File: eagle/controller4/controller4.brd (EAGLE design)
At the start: 47.9 x 64.8 mm, 62 parts, among them J4 USB-MICROB, J7 2X6 FEMALE, Q3 check_pins, X1 1501_04

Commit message: controller4 progress
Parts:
- removed HIGHSIDESWITCH: (no value), SparkFun-DiscreteSemi:TO220V
- added Q2: FDD4141TO252, transistor-fet:TO252
- moved SH 35.2 mm to (40.6, 13.6), turned to 180 degrees
- moved J5 17.8 mm to (43.2, 24.1)
- moved CONV_X_VCC 17.8 mm to (41.9, 35.6)
- moved J6 16.6 mm to (43.2, 16.5)
- moved R8 12.6 mm to (33.0, 10.2), turned to 90 degrees
- moved R9 8.98 mm to (30.5, 10.2), turned to 270 degrees
- moved DISP 2.54 mm to (25.4, 2.54)
- moved T_HSS 1.80 mm to (36.8, 34.3), turned to 270 degrees
- moved J3 1.27 mm to (39.4, 6.35)
- moved S1 1.27 mm to (43.9, 6.35)
- moved VD1 1.27 mm to (36.8, 55.9)
- moved X1 1.27 mm to (48.3, 61.0)
- moved R18 1.27 mm to (30.5, 33.0)
- moved SHTR 1.27 mm to (29.2, 62.2)
- moved R17 1.27 mm to (34.3, 29.2)
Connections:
- net BATT_VCC: now also Q2.2; no longer HIGHSIDESWITCH.3
- net CAM_OUT: now also Q2.3; no longer HIGHSIDESWITCH.2
- net N$36: now also Q2.1; no longer HIGHSIDESWITCH.1
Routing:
- net DISP_RST: track 46.1 -> 60.8 mm, vias 3 -> 1
- net GND: track 308.1 -> 298.0 mm
- net BATT_VCC: track 44.5 -> 35.9 mm, vias 0 -> 1
- net TX: track 28.6 -> 20.5 mm, vias 4 -> 0
- net GNDA: track 17.1 -> 9.05 mm
- net N$31: track 3.08 -> 10.4 mm
- net N$36: track 14.6 -> 8.84 mm
- net CAM_OUT: track 15.6 -> 9.88 mm
- net VCC: track 201.0 -> 197.2 mm
- net SCL: track 53.7 -> 57.1 mm, vias 2 -> 4
- net MOSI: track 24.5 -> 27.6 mm
- net BTN2: track 31.9 -> 33.7 mm
- net N$34: track 15.5 -> 14.1 mm
- net CAM_EN: track 6.91 -> 5.59 mm
- net N$6: track 5.14 -> 6.43 mm
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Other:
- board size 47.9 x 64.8 mm -> 46.7 x 64.8 mm

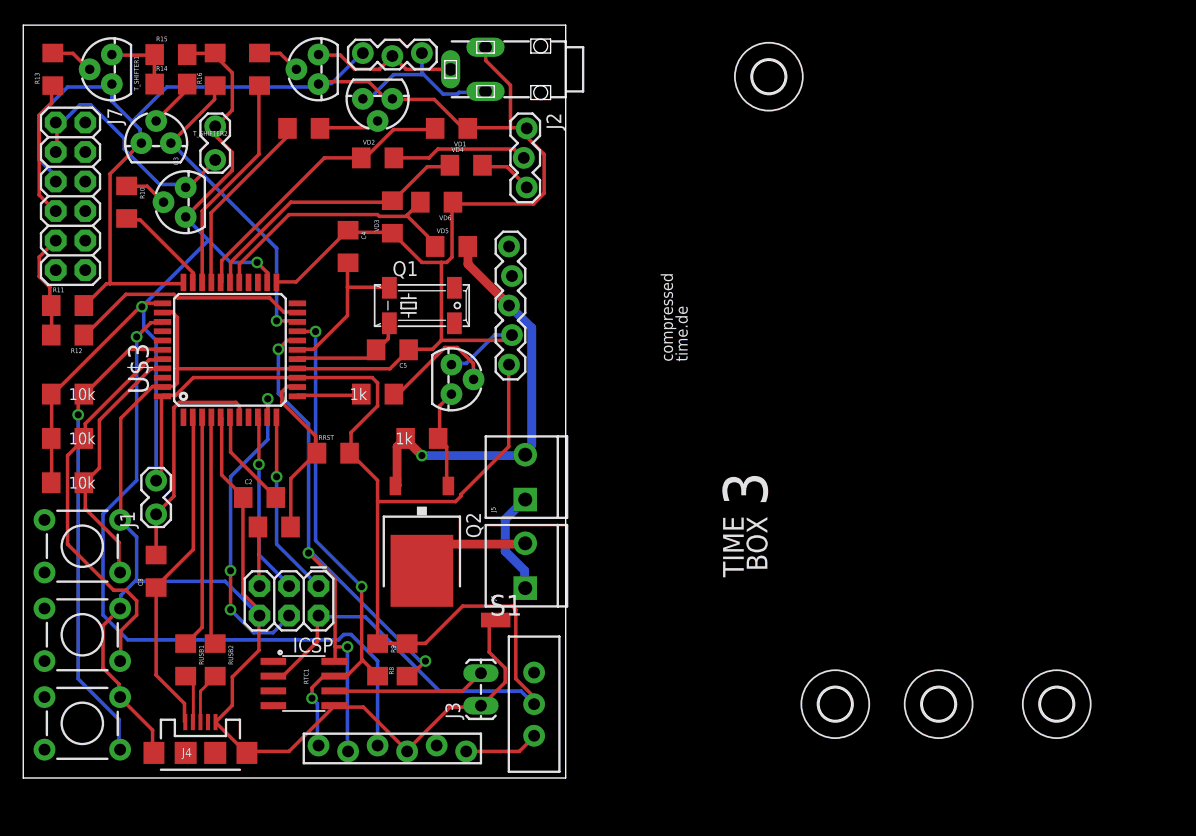
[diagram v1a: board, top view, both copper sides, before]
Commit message: controller4: added switch (battery -> USB)
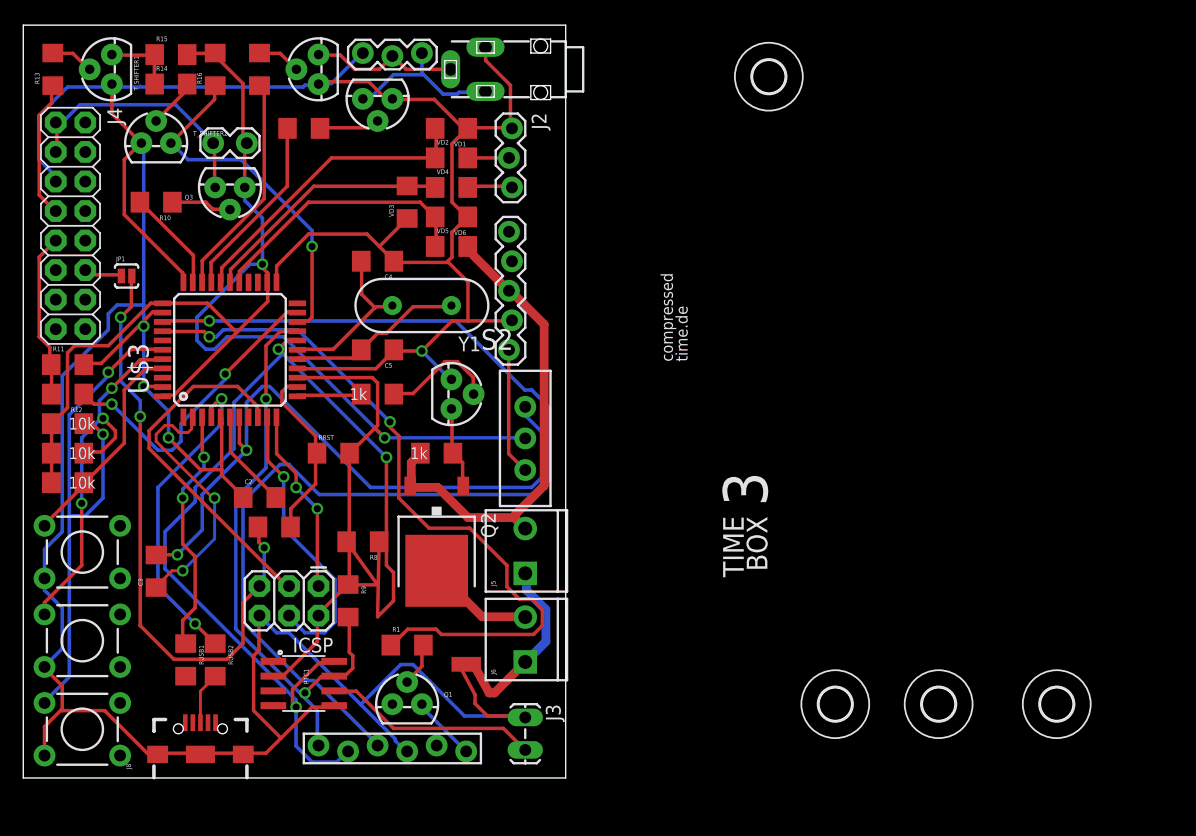
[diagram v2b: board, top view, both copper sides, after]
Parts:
- removed J1: (no value), SparkFun-Connectors:1X02_LOCK
- removed J7: 2X6 FEMALE, SparkFun-Connectors:2X6
- removed S1: (no value), SparkFun-Electromechanical:SWITCH-SPDT_LOCK.007S
- added J8: (no value), SparkFun-Connectors:USB-B-MICRO-SMD_V03
- added JP1: JUMPER-PAD-2-NOYES_SILK, SparkFun-Passives:PAD-JUMPER-2-NO_YES_SILK
- added R1: (no value), SparkFun-Resistors:1206
- added S2: (no value), SparkFun-Electromechanical:SWITCH-SPDT_LOCK.007S
- added Y1: (no value), SparkFun-FreqCtrl:HC49US
- J4: value USB-MICROB -> (none); device SparkFun-Connectors:USB-MICROB -> SparkFun-Connectors:2X8
- Q1: value (none) -> check_pins; device adafruit:MM20SS -> SparkFun-DiscreteSemi:TO-92
- moved J4 55.6 mm to (2.79, 56.4), turned to 270 degrees
- moved Q1 34.3 mm to (33.0, 6.35)
- moved R8 10.9 mm to (29.2, 20.3), turned to 180 degrees
- moved J6 6.35 mm to (43.2, 10.2)
- moved J5 6.35 mm to (43.2, 17.8)
- moved VD2 6.35 mm to (36.8, 53.3)
- moved R9 5.68 mm to (27.9, 15.2)
- moved R11 5.08 mm to (3.81, 35.6)
- moved R12 5.08 mm to (3.81, 33.0)
- moved SH 4.58 mm to (38.1, 9.78)
- moved J3 4.02 mm to (43.2, 5.08), turned to 270 degrees
- moved Q3 4.02 mm to (17.8, 50.8), turned to 180 degrees
- moved C4 2.84 mm to (30.5, 44.5), turned to 180 degrees
- moved RB3 2.54 mm to (3.81, 30.5)
- moved R10 2.54 mm to (11.4, 49.5), turned to 180 degrees
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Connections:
- removed net N$16: J7.6
- new net CONV_5V: CONV_X_VCC.1, S2.3
- new net N$12: Q1.2, R1.2
- new net N$7: J4.12, JP1.1
- net +5V: now also J4.1, J4.3; no longer J7.1, J7.3
- net DISP_EN: now also R1.1
- net GND: now also J4.5, J8.GND, J8.SHIELD1, J8.SHIELD2, J8.SHIELD3; no longer J4.GND, J4.MT1, J4.MT2, J7.5
- net N$10: now also S2.1; no longer J1.1
- net N$11: now also J8.D-; no longer J4.D-
- net N$14: now also J8.D+; no longer J4.D+
- net N$22: now also J8.VBUS; no longer J4.VBUS
- net N$6: now also Q1.3; no longer S1.3
- net N$8: now also Y1.2; no longer Q1.4
- net N$9: now also Y1.1; no longer Q1.1
- net RST: now also JP1.2
- net VCC: now also S2.2; no longer CONV_X_VCC.1, J1.2, S1.2
- net ZRX: now also J4.9; no longer J7.9
- net ZTX: now also J4.7; no longer J7.7
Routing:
- net DISP_EN: track 0.00 -> 63.0 mm, vias 0 -> 2
- net RST: track 5.12 -> 52.8 mm, vias 0 -> 3
- net VCC: track 197.2 -> 154.8 mm
- net DISP_RST: track 60.8 -> 98.3 mm
- net N$10: track 20.2 -> 57.1 mm, vias 0 -> 2
- net SCL: track 57.1 -> 90.4 mm, vias 4 -> 3
- net GND: track 298.0 -> 327.7 mm, vias 0 -> 4
- net SCK: track 15.6 -> 31.1 mm, vias 1 -> 0
- net CONV_5V: track 0.00 -> 10.9 mm
- net N$3: track 11.8 -> 3.55 mm
- net N$5: track 19.6 -> 27.4 mm, vias 0 -> 2
- net SDA: track 44.0 -> 51.5 mm, vias 3 -> 2
- net GNDA: track 9.05 -> 16.1 mm
- net BTN3: track 40.7 -> 47.3 mm, vias 1 -> 2
- net TX: track 20.5 -> 26.5 mm, vias 0 -> 2
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
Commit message: controller4: changed layout
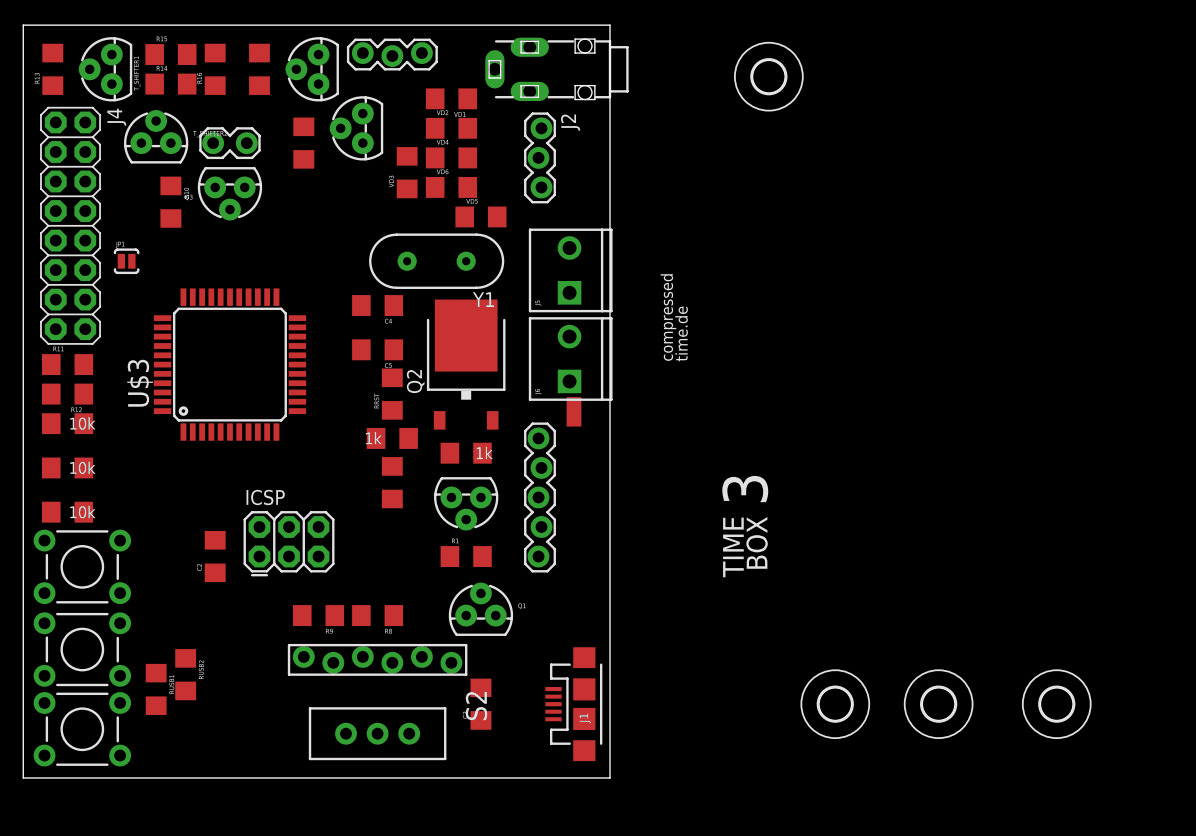
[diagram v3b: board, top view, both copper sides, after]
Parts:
- removed J3: (no value), SparkFun-Connectors:1X02_LOCK_LONGPADS
- removed J8: (no value), SparkFun-Connectors:USB-B-MICRO-SMD_V03
- removed RTC1: DS3231M, SparkFun-DigitalIC:SOIC8
- added J1: USB-MICROB, SparkFun-Connectors:USB-MICROB
- moved C3 30.2 mm to (39.4, 6.35)
- moved S2 28.4 mm to (30.5, 3.81), turned to 270 degrees
- moved J6 24.4 mm to (47.0, 34.3)
- moved J5 24.4 mm to (47.0, 41.9)
- moved SH 23.6 mm to (47.4, 31.5), turned to 270 degrees
- moved CONV_X_VCC 18.0 mm to (44.5, 19.1)
- moved Q2 15.5 mm to (38.1, 35.6), turned to 0 degrees
- moved C1 10.9 mm to (31.8, 25.4), turned to 90 degrees
- moved Q1 9.92 mm to (39.4, 14.0)
- moved R1 9.16 mm to (38.1, 19.1)
- moved T_HSS 8.98 mm to (38.1, 24.1), turned to 180 degrees
- moved DISP 7.73 mm to (24.1, 10.2)
- moved RRST 7.18 mm to (31.8, 33.0), turned to 90 degrees
- moved R8 6.48 mm to (30.5, 14.0)
- moved C2 6.35 mm to (16.5, 19.1), turned to 90 degrees
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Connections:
- removed net N$10: C3.2, S2.1, U$3.7
- removed net N$25: J3.2, RTC1.6
- removed net RTC_RST: RTC1.4
- net BTN1: now also U$3.39; no longer U$3.41
- net BTN2: now also U$3.38; no longer U$3.40
- net BTN3: now also U$3.37; no longer U$3.39
- net CONV_5V: now also S2.1; no longer S2.3
- net DISP_EN: now also U$3.40; no longer U$3.37
- net DISP_RST: now also U$3.41; no longer U$3.36
- net GND: now also C3.2, J1.GND, J1.MT1, J1.MT2; no longer J3.1, J8.GND, J8.SHIELD1, J8.SHIELD2, J8.SHIELD3, RTC1.5
- net N$11: now also J1.D-; no longer J8.D-
- net N$14: now also J1.D+; no longer J8.D+
- net N$22: now also J1.VBUS, S2.3, U$3.7; no longer J8.VBUS, U$3.2
- net SCL: no longer RTC1.8
- net SDA: no longer RTC1.7
- net VCC: now also Q1.1, U$3.2, U$3.42; no longer RTC1.2
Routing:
- net GND: track 327.7 -> 0.00 mm, vias 4 -> 0
- net VCC: track 154.8 -> 0.00 mm, vias 2 -> 0
- net DISP_RST: track 98.3 -> 0.00 mm, vias 1 -> 0
- net SCL: track 90.4 -> 0.00 mm, vias 3 -> 0
- net DISP_EN: track 63.0 -> 0.00 mm, vias 2 -> 0
- net N$10: track 57.1 -> 0.00 mm, vias 2 -> 0
- net RST: track 52.8 -> 0.00 mm, vias 3 -> 0
- net SDA: track 51.5 -> 0.00 mm, vias 2 -> 0
- net BTN3: track 47.3 -> 0.00 mm, vias 2 -> 0
- net BATT_VCC: track 41.8 -> 0.00 mm
- net BTN2: track 33.0 -> 0.00 mm, vias 3 -> 0
- net SCK: track 31.1 -> 0.00 mm
- net RX: track 30.7 -> 0.00 mm, vias 1 -> 0
- net N$5: track 27.4 -> 0.00 mm, vias 2 -> 0
- net TX: track 26.5 -> 0.00 mm, vias 2 -> 0
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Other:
- board size 46.7 x 64.8 mm -> 50.5 x 64.8 mm

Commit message: controller4: moved display to the upper half
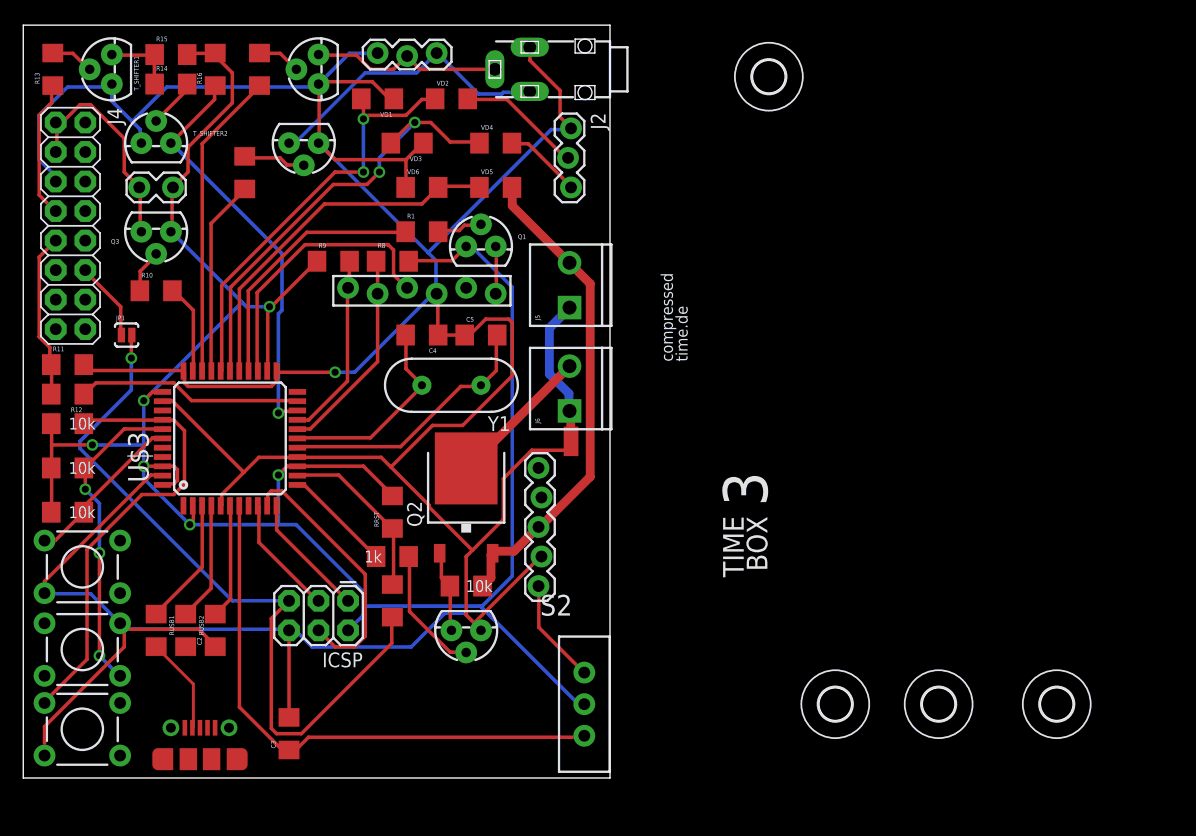
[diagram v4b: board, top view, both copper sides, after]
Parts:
- removed J1: USB-MICROB, SparkFun-Connectors:USB-MICROB
- added U$1: USB-CON-5PIN-105017-0001, GeekAmmo:USB-MICRO-MOLEX-105017-0001
- Q2: value FDD4141TO252 -> (none)
- R17: value 1k -> 10k
- moved DISP 32.0 mm to (27.9, 41.9)
- moved Q1 31.8 mm to (39.4, 45.7)
- moved R8 30.5 mm to (31.8, 44.5), turned to 0 degrees
- moved R9 30.5 mm to (26.7, 44.5), turned to 0 degrees
- moved R1 28.2 mm to (34.3, 47.0)
- moved S2 18.0 mm to (48.3, 6.35), turned to 0 degrees
- moved C3 16.7 mm to (22.9, 3.81)
- moved Q2 11.4 mm to (38.1, 24.1)
- moved R17 11.4 mm to (38.1, 16.5)
- moved T_HSS 11.4 mm to (38.1, 12.7)
- moved Y1 10.7 mm to (36.8, 33.8)
- moved RRST 10.2 mm to (31.8, 22.9)
- moved R18 10.2 mm to (31.8, 19.1)
- moved C1 10.2 mm to (31.8, 15.2)
- moved C5 8.98 mm to (39.4, 38.1), turned to 0 degrees
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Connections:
- net CELL1: now also U$3.29, VD1.2, VD2.1; no longer U$3.28, VD3.2, VD4.1
- net CELL2: now also U$3.28, VD3.2, VD4.1; no longer U$3.29, VD1.2, VD2.1
- net DISP_EN: now also U$3.26; no longer U$3.40
- net DISP_RST: now also U$3.25; no longer U$3.41
- net GND: now also U$1.5; no longer J1.GND, J1.MT1, J1.MT2
- net N$11: now also U$1.2; no longer J1.D-
- net N$14: now also U$1.3; no longer J1.D+
- net N$22: now also U$1.1; no longer J1.VBUS
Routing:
- net GND: track 0.00 -> 330.1 mm, vias 0 -> 1
- net VCC: track 0.00 -> 190.8 mm, vias 0 -> 6
- net RST: track 0.00 -> 62.7 mm, vias 0 -> 1
- net N$22: track 0.00 -> 49.0 mm
- net BATT_VCC: track 0.00 -> 42.0 mm
- net BTN3: track 0.00 -> 39.2 mm
- net CELL2: track 0.00 -> 38.8 mm, vias 0 -> 2
- net CELL1: track 0.00 -> 36.8 mm, vias 0 -> 2
- net RX: track 0.00 -> 35.5 mm, vias 0 -> 1
- net VD_DIRECT: track 0.00 -> 31.4 mm
- net BTN2: track 0.00 -> 27.3 mm, vias 0 -> 3
- net CAM2: track 0.00 -> 26.6 mm
- net N$34: track 0.00 -> 25.5 mm
- net DISP_RST: track 0.00 -> 24.2 mm
- net N$9: track 0.00 -> 23.0 mm
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
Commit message: controller4: intermediate
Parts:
- removed BTN_DW, BTN_UP, BTN_X: (no value), SparkFun-Retired:TACTILE-PTH
- added RB4, RB5: 10k, SparkFun-Resistors:1206
- added S1: (no value), SparkFun-Electromechanical:JOYSTICK_MINI
- moved H3 62.1 mm to (95.9, 6.99)
- moved SHTR 59.7 mm to (31.8, 2.54)
- moved C3 59.5 mm to (34.3, 62.2), turned to 0 degrees
- moved S2 59.2 mm to (25.4, 61.0), turned to 270 degrees
- moved U$1 58.4 mm to (40.1, 55.9), turned to 90 degrees
- moved T_CAM4 57.2 mm to (27.9, 3.81)
- moved X1 57.1 mm to (52.1, 3.81)
- moved R20 50.9 mm to (22.9, 10.2), turned to 90 degrees
- moved T_CAM3 50.9 mm to (21.6, 3.81), turned to 90 degrees
- moved Q1 48.3 mm to (11.4, 6.35)
- moved VD2 48.3 mm to (35.6, 10.2)
- moved VD4 47.3 mm to (35.6, 7.62)
- moved VD1 47.0 mm to (29.2, 11.4)
- moved DISP 46.9 mm to (2.54, 2.54)
- moved VD3 45.9 mm to (29.2, 8.89)
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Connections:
- removed net BTN1: BTN_UP.4, RB1.1, U$3.39
- removed net BTN2: BTN_DW.4, RB2.1, U$3.38
- removed net BTN3: BTN_X.4, RB3.1, U$3.37
- new net BTN_C: RB3.1, S1.CTR, U$3.39
- new net BTN_D: RB1.1, S1.D, U$3.36
- new net BTN_L: RB4.1, S1.C, U$3.38
- new net BTN_R: RB5.1, S1.B, U$3.37
- new net BTN_U: RB2.1, S1.A, U$3.40
- new net FOO: U$3.32
- net CAM_EN: now also U$3.41; no longer U$3.12
- net GND: now also S1.GND; no longer BTN_DW.2, BTN_UP.2, BTN_X.2
- net VCC: now also RB4.2, RB5.2
- net ZERO_EN: now also U$3.12; no longer U$3.32
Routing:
- net GND: track 330.1 -> 0.00 mm, vias 1 -> 0
- net VCC: track 190.8 -> 0.00 mm, vias 6 -> 0
- net RST: track 62.7 -> 0.00 mm, vias 1 -> 0
- net N$22: track 49.0 -> 0.00 mm
- net BATT_VCC: track 42.0 -> 0.00 mm
- net BTN3: track 39.2 -> 0.00 mm
- net CELL2: track 38.8 -> 0.00 mm, vias 2 -> 0
- net CELL1: track 36.8 -> 0.00 mm, vias 2 -> 0
- net RX: track 35.5 -> 0.00 mm, vias 1 -> 0
- net VD_DIRECT: track 31.4 -> 0.00 mm
- net BTN2: track 27.3 -> 0.00 mm, vias 3 -> 0
- net CAM2: track 26.6 -> 0.00 mm
- net N$34: track 25.5 -> 0.00 mm
- net DISP_RST: track 24.2 -> 0.00 mm
- net N$9: track 23.0 -> 0.00 mm
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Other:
- outline, holes or cut-outs redrawn
